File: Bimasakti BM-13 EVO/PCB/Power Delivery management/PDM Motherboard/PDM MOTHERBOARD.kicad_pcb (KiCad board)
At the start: 2 copper layers, 86.5 x 81.4 mm, 28 parts

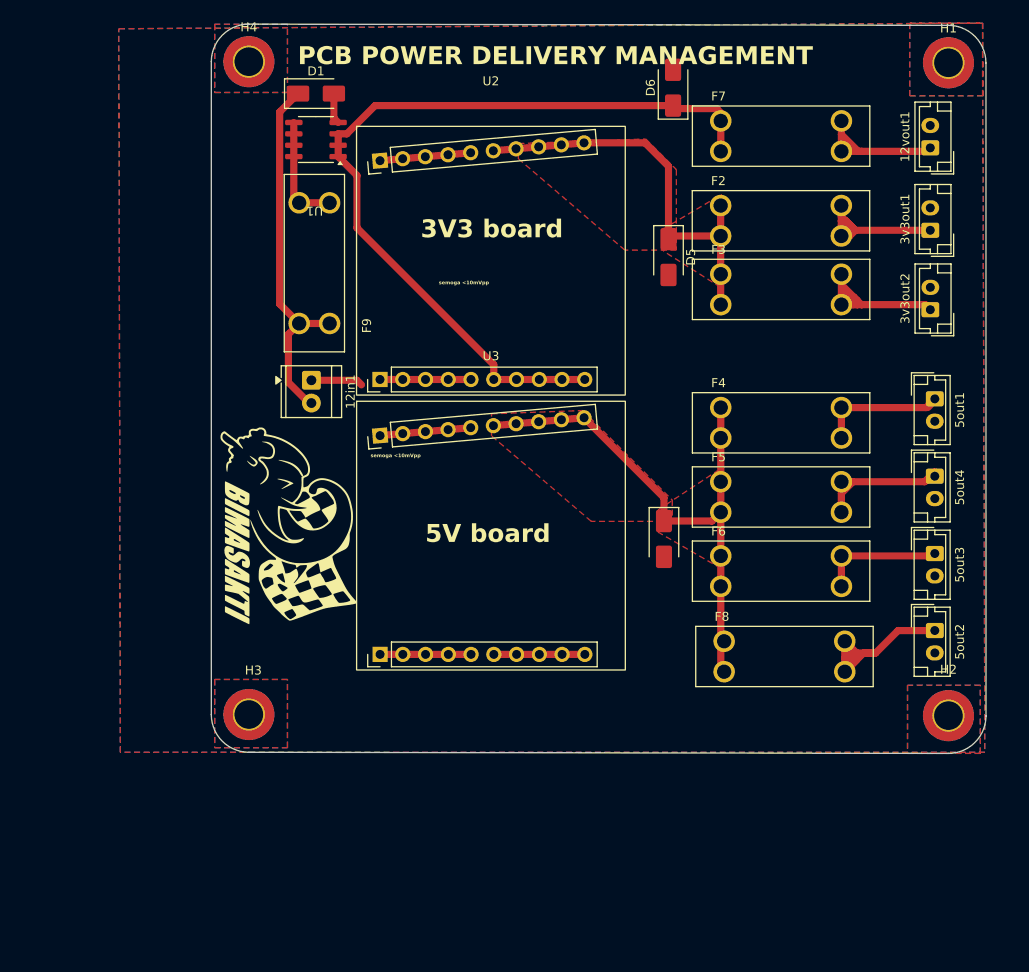
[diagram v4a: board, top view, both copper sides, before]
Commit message: pdm selesai ril, tv board sudah bagus kurang cek (mungkin ganti konektor)
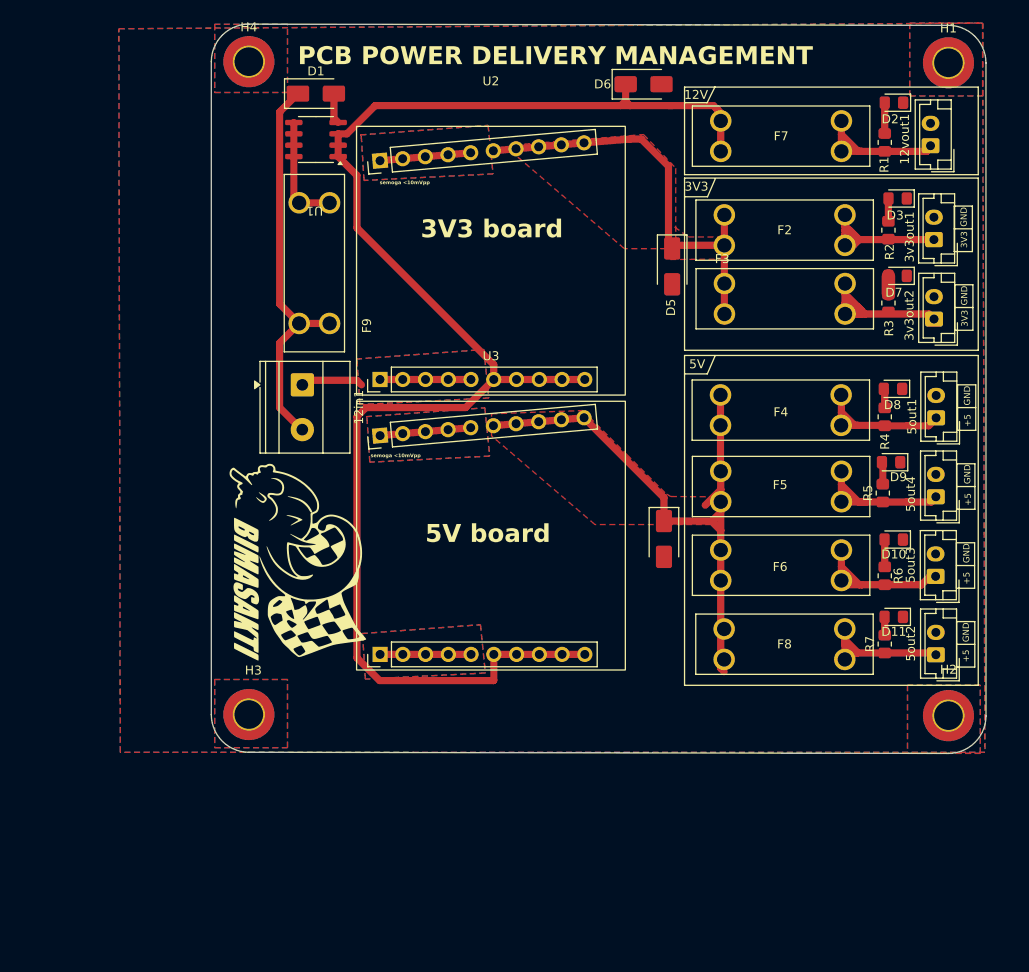
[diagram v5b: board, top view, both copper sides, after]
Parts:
- added D10: LED, LED_SMD:LED_0805_2012Metric_Pad1.15x1.40mm_HandSolder, F.Cu at (147.3, 72.6)
- added D11: LED, LED_SMD:LED_0805_2012Metric_Pad1.15x1.40mm_HandSolder, F.Cu at (147.3, 81.3)
- added D2: LED, LED_SMD:LED_0805_2012Metric_Pad1.15x1.40mm_HandSolder, F.Cu at (147.3, 23.9)
- added D3: LED, LED_SMD:LED_0805_2012Metric_Pad1.15x1.40mm_HandSolder, F.Cu at (147.7, 34.6)
- added D7: LED, LED_SMD:LED_0805_2012Metric_Pad1.15x1.40mm_HandSolder, F.Cu at (147.7, 43.2)
- added D8: LED, LED_SMD:LED_0805_2012Metric_Pad1.15x1.40mm_HandSolder, F.Cu at (147.2, 55.8)
- added D9: LED, LED_SMD:LED_0805_2012Metric_Pad1.15x1.40mm_HandSolder, F.Cu at (147.0, 64.0)
- added R1: 1k, Resistor_SMD:R_0805_2012Metric_Pad1.20x1.40mm_HandSolder, F.Cu at (146.3, 28.3)
- added R2: 220R, Resistor_SMD:R_0805_2012Metric_Pad1.20x1.40mm_HandSolder, F.Cu at (146.7, 38.1)
- added R3: 220R, Resistor_SMD:R_0805_2012Metric_Pad1.20x1.40mm_HandSolder, F.Cu at (146.7, 46.2)
- added R4: 330R, Resistor_SMD:R_0805_2012Metric_Pad1.20x1.40mm_HandSolder, F.Cu at (146.3, 58.9)
- added R5: 330R, Resistor_SMD:R_0805_2012Metric_Pad1.20x1.40mm_HandSolder, F.Cu at (146.1, 67.5)
- added R6: 330R, Resistor_SMD:R_0805_2012Metric_Pad1.20x1.40mm_HandSolder, F.Cu at (146.3, 76.7)
- added R7: 330R, Resistor_SMD:R_0805_2012Metric_Pad1.20x1.40mm_HandSolder, F.Cu at (146.3, 84.3)
- 12in1: footprint TerminalBlock_TE-Connectivity:TerminalBlock_TE_282834-2_1x02_P2.54mm_Horizontal -> TerminalBlock_Phoenix:TerminalBlock_Phoenix_MKDS-1,5-2_1x02_P5.00mm_Horizontal
- moved G*** 4.19 mm to (80.8, 75.2)
- moved D6 3.31 mm to (119.4, 21.8), turned to 0 degrees
- moved 5out2 2.71 mm to (152.0, 85.5), turned to 90 degrees
- moved 5out3 2.55 mm to (152.0, 76.8), turned to 90 degrees
- moved 5out4 2.30 mm to (152.0, 67.9), turned to 90 degrees
- moved 5out1 2.13 mm to (152.0, 59.1), turned to 90 degrees
- moved F4 1.42 mm to (134.7, 58.2)
- moved F8 1.37 mm to (135.1, 84.3)
- moved F5 1.17 mm to (134.7, 66.7)
- moved 12in1 1.14 mm to (81.3, 55.4)
- moved 3v3out1 1.12 mm to (151.8, 39.2)
- moved F3 1.12 mm to (135.1, 45.8)
- moved F2 1.12 mm to (135.1, 38.1)
- moved D5 1.12 mm to (122.6, 42.1)
- moved 3v3out2 1.12 mm to (151.8, 48.0)
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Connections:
- net +12 renamed 12tobuck
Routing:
- net 12tobuck: track 104.4 -> 170.9 mm
- net Net-(5out2-Pin_1): track 27.5 -> 18.6 mm
- net 5Vin: track 61.8 -> 66.0 mm
- net Net-(5out3-Pin_1): track 14.0 -> 17.7 mm
- net Net-(D2-A): track 0.00 -> 3.43 mm
- net Net-(12in1-Pin_2): track 41.4 -> 44.7 mm
- net Net-(D10-A): track 0.00 -> 3.06 mm
- net Net-(D3-A): track 0.00 -> 2.54 mm
- net Net-(D9-A): track 0.00 -> 2.48 mm
- net Net-(D8-A): track 0.00 -> 2.17 mm
- net Net-(5out1-Pin_1): track 14.6 -> 16.7 mm
- net Net-(D11-A): track 0.00 -> 2.04 mm
- net Net-(D7-A): track 0.00 -> 2.03 mm
- net Net-(12vout1-Pin_1): track 16.6 -> 17.8 mm
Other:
- board text added: "+5"
- board text added: "12V"
- board text added: "3V3"
- board text added: "5V"
- board text added: "GND"

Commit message: buat placeholder baru dan ganti konektor
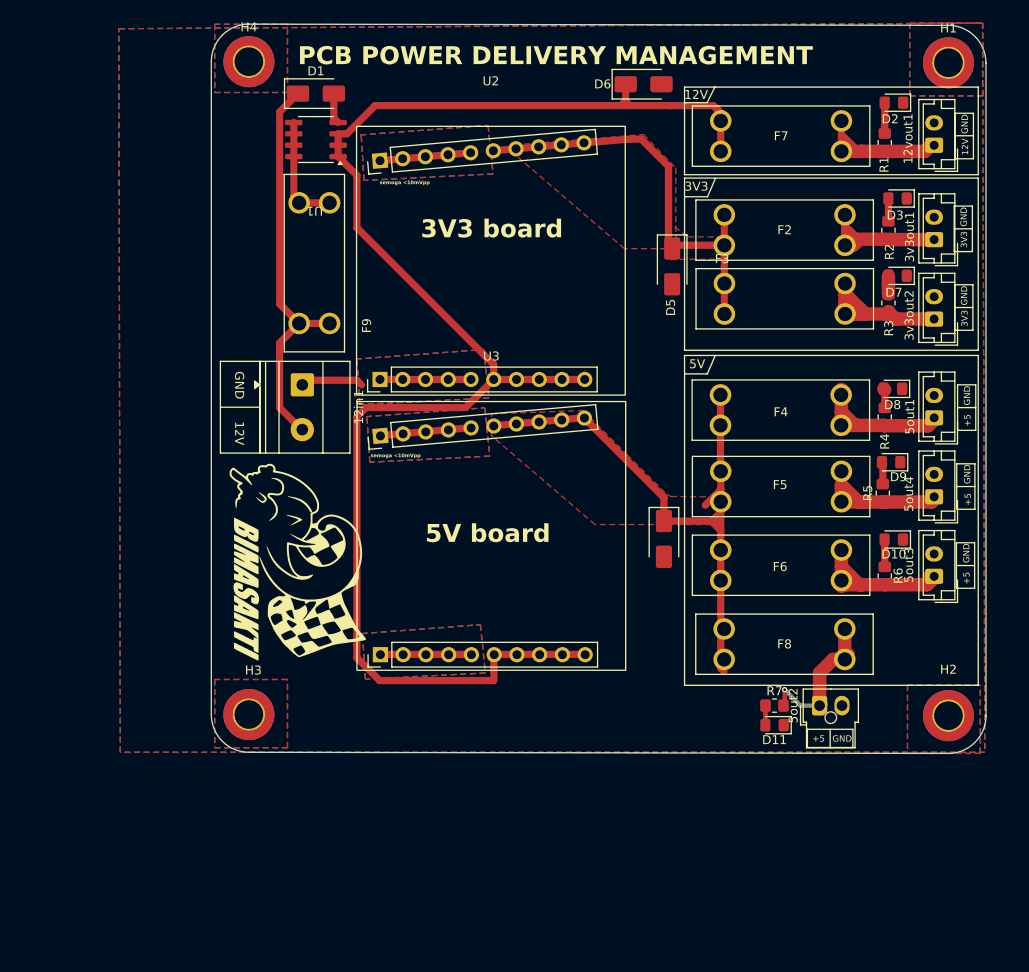
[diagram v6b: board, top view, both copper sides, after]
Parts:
- 5out2: footprint Connector_JST:JST_EH_B2B-EH-A_1x02_P2.50mm_Vertical -> Connector_Molex:Molex_Nano-Fit_105309-xx02_1x02_P2.50mm_Vertical
- moved D11 18.0 mm to (134.0, 93.4)
- moved 5out2 14.2 mm to (139.0, 91.2)
- moved R7 14.1 mm to (134.0, 91.2), turned to 180 degrees
- moved 12vout1 0.41 mm to (151.8, 28.6)
- moved 5out1 0.22 mm to (151.8, 59.1)
- moved 5out4 0.19 mm to (151.8, 67.9)
- moved 5out3 0.17 mm to (151.8, 76.8)
- moved U3 0.05 mm to (102.4, 52.7)
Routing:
- net Net-(5out2-Pin_1): track 18.6 -> 19.7 mm, vias 0 -> 1
- net Net-(5out3-Pin_1): track 17.7 -> 18.6 mm
- net Net-(12vout1-Pin_1): track 17.8 -> 16.9 mm

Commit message: update
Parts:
- removed 3v3out2: ~, Connector_JST:JST_EH_B2B-EH-A_1x02_P2.50mm_Vertical
- added 5out5: ~, Connector_JST:JST_EH_B2B-EH-A_1x02_P2.50mm_Vertical, F.Cu at (151.8, 49.7)
- added D12: LED, LED_SMD:LED_0805_2012Metric_Pad1.15x1.40mm_HandSolder, F.Cu at (75.2, 50.8)
- added G***: LOGO, 0_logo:qrcode, F.Cu at (101.1, 42.2)
- added R8: 1k, Resistor_SMD:R_0805_2012Metric_Pad1.20x1.40mm_HandSolder, F.Cu at (75.7, 44.7)
- moved R3 4.07 mm to (146.7, 50.3)
- moved D7 4.04 mm to (147.7, 47.2)
- moved F3 3.55 mm to (134.6, 49.3)
- moved D5 1.19 mm to (121.9, 41.1)
- moved 5out1 0.31 mm to (151.8, 58.7)
- moved 5out4 0.13 mm to (151.8, 67.7)
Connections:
- F3 pad 1_1: 3Vin -> 5Vin
- F3 pad 1_2: 3Vin -> 5Vin
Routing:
- net 5Vin: track 66.0 -> 74.9 mm
- net 3Vin: track 46.2 -> 38.5 mm
- net 12tobuck: track 170.9 -> 178.4 mm
- net Net-(5out5-Pin_1): track 20.3 -> 14.7 mm
- net Net-(D12-A): track 0.00 -> 4.99 mm, vias 0 -> 2
- net Net-(12in1-Pin_2): track 44.7 -> 48.4 mm, vias 0 -> 2
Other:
- board text added: "designed by putpluto"
- board text added: "they ridiculed me for this unusual shape it turns out that it really is stupid they were right and im just autistic"

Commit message: tv dengan pdm kecil
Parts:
- removed F3: 3557-2, 0_FUSE:0_FUSE_3557-2
- removed the G*** at (101.1, 42.2)
- moved H2 76.0 mm to (77.9, 83.5)
- moved H3 71.7 mm to (77.9, 20.5)
- moved H4 69.6 mm to (144.9, 20.5)
- moved H1 64.6 mm to (144.9, 83.5)
- moved F8 36.2 mm to (128.1, 48.8)
- moved D1 27.8 mm to (89.0, 50.0)
- moved U1 14.3 mm to (90.4, 47.5)
- moved D11 13.3 mm to (124.9, 83.7), turned to 0 degrees
- moved R7 11.9 mm to (127.0, 81.5)
- moved 5out2 11.7 mm to (132.2, 81.6)
- moved R8 9.70 mm to (83.0, 51.1), turned to 180 degrees
- moved 12vout1 8.93 mm to (143.0, 30.0)
- moved 3v3out1 8.86 mm to (143.0, 40.0)
- moved 5out1 8.83 mm to (143.0, 59.0)
- moved 5out3 8.83 mm to (143.0, 77.0)
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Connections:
- 5out2 pad 1: Net-(5out2-Pin_1) -> /5v_f3
- 5out3 pad 1: Net-(5out3-Pin_1) -> /5v_f3
- F6 pad 2_1: Net-(5out3-Pin_1) -> /5v_f3
- F6 pad 2_2: Net-(5out3-Pin_1) -> /5v_f3
- F8 pad 2_1: Net-(5out2-Pin_1) -> Net-(5out5-Pin_1)
- F8 pad 2_2: Net-(5out2-Pin_1) -> Net-(5out5-Pin_1)
- H3 pad 1: GND -> (no net)
- H4 pad 1: GND -> (no net)
- R6 pad 1: Net-(5out3-Pin_1) -> /5v_f3
- R7 pad 1: Net-(5out2-Pin_1) -> /5v_f3
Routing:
- net GND: track 49.9 -> 4.21 mm
- net 12tobuck: track 178.4 -> 211.6 mm
- net Net-(12in1-Pin_2): track 48.4 -> 24.7 mm, vias 2 -> 0
- net /5v_f3: track 0.00 -> 22.7 mm
- net Net-(5out2-Pin_1): track 19.7 -> 0.00 mm, vias 1 -> 0
- net Net-(5out3-Pin_1): track 18.6 -> 0.00 mm
- net 5Vin: track 74.9 -> 58.2 mm
- net Net-(5out4-Pin_1): track 18.1 -> 9.77 mm
- net 3Vin: track 38.5 -> 31.5 mm
- net Net-(3v3out1-Pin_1): track 19.7 -> 12.7 mm
- net Net-(12vout1-Pin_1): track 16.9 -> 11.9 mm
- net Net-(5out1-Pin_1): track 16.8 -> 13.3 mm
- net Net-(D12-A): track 4.99 -> 1.78 mm, vias 2 -> 0
- net Net-(U1-D): track 12.6 -> 14.6 mm
- net Net-(D2-A): track 3.43 -> 1.79 mm
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- removed copper zone on F.Cu, net 3Vin
- removed copper zone on F.Cu, net 5Vin
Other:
- board size 86.5 x 81.4 mm -> 77 x 73.1 mm
- board text added: "PCB Power Delivery Management"
- board text removed: "5V"
- board text removed: "PCB POWER DELIVERY MANAGEMENT"
